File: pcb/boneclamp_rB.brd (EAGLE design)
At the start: 160 x 100 mm, 65 parts, among them IC1 24C, U1 AD7656YSTZ, U2 AD5754RBREZ, U3 SN74ABT541BDW, U4 ADP3303ARZ-5, U5 ADP3303ARZ-5, U6 ADR431BRZ, U7 AD7682BCPZ

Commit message: More changes to circuit
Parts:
- removed U$26: LM1085, boneclamp:TO263-3
- removed U$28: SCREW3, boneclamp:SCREW3
- added C21: 0.1uF, rcl:C0603
- added C25, C28: 10uF, rcl:C1206
- added U8: TPS63700DRCT, ti-extended:SON50P300X300X100-11N
- C19, C20: value 10uF -> 0.1uF; device rcl:C1206 -> rcl:C0603
- U2: value AD5754RBREZ -> ADP3303ARZ-5; device analog-devices-01:SOP65P640X120-25N -> analog-devices-01:SOIC127P600X175-8N
- moved C20 148.6 mm to (-85.1, -52.1)
- moved C19 137.1 mm to (-72.4, -44.5)
- moved U2 134.0 mm to (-82.5, -35.6), turned to 0 degrees
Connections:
- removed net +12V: C19.1, U$26.3
- removed net -12V: U$28.P$3
- removed net EPAD: U2.25
- removed net PGND: U$28.P$2
- new net AVSS: C20.1, C21.1, C28.1, U2.1, U2.2
- new net N$26: C20.2, U2.3
- new net VIN: U8.3
- net AGND: now also C19.2, C21.2, C25.2, C28.2, U2.4
- net BB_5V: now also C19.1, C25.1, U2.5, U2.7, U2.8
- net DAC_A: no longer U2.3
- net DAC_B: no longer U2.4
- net DAC_C: no longer U2.23
- net DAC_D: no longer U2.22
- net DGND: no longer C19.2, C20.2, U$26.1
- net DVCC: no longer U2.14
- net N$24: no longer U2.17
- net N$7: no longer U2.16
- net N$8: no longer U2.9
- net VDD: no longer U2.24
- net VDD_BB: no longer C20.1, U$26.2, U$26.TAB
- net VSS: no longer U2.1

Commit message: Worked a bit on the schematic
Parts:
- removed C23: 10uF, rcl:C1206
- removed C24, C26, C27: 0.1uF, rcl:C0603
- removed JP5: (no value), jumper:JP2
- removed JP6: (no value), jumper:JP1
- removed TP5: TPB1,27, testpad:B1,27
- removed U3: SN74ABT541BDW, ti-extended:SOIC127P1030X265-20N
- removed U6: ADR431BRZ, analog-devices-01:SOIC127P600X175-8N
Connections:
- removed net N$23: JP6.1
- removed net N$25: C26.1, U6.1
- removed net VCC: U3.20
- removed net VREF_OUT: C27.1, JP5.3, JP6.2, TP5.TP, U6.6
- net AGND: no longer C23.2, C24.2, C26.2, U6.4
- net VDD: no longer C23.1, C24.1, U6.2
- net VREF_2.5V: no longer JP5.2
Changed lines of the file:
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@@
 <attribute name="OC_FARNELL" value="1274233" x="194.31" y="153.67" size="1.778" layer="27" rot="R90" display="off"/>
-</element>
-<element name="U3" library="ti-extended" package="SOIC127P1030X265-20N" value="SN74ABT541BDW" x="76.2" y="19.05" rot="R90">
-<attribute name="PACKAGE" value="SOIC-20" x="173.99" y="109.22" size="1.778" layer="27" rot="R90" display="off"/>
-<attribute name="OC_NEWARK" value="85F222" x="173.99" y="109.22" size="1.778" layer="27" rot="R90" display="off"/>
-<attribute name="MPN" value="SN74ABT541BDW" x="173.99" y="109.22" size="1.778" layer="27" rot="R90" display="off"/>
-<attribute name="SUPPLIER" value="Texas Instruments" x="173.99" y="109.22" size="1.778" layer="27" rot="R90" display="off"/>
-<attribute name="OC_FARNELL" value="9590170" x="173.99" y="109.22" size="1.778" layer="27" rot="R90" display="off"/>
 </element>
 <element name="BCIO" library="adafruit" package="HDF15H" value="F15-SHEILD" x="27.305" y="74.93" rot="R180"/>
@@
 <element name="JP3" library="jumper" package="JP1" value="" x="6.35" y="-16.51"/>
 <element name="JP4" library="jumper" package="JP1" value="" x="6.35" y="-24.13"/>
-<element name="U6" library="analog-devices-01" package="SOIC127P600X175-8N" value="ADR431BRZ" x="-46.99" y="48.26">
-<attribute name="PACKAGE" value="SOIC-8" x="-46.99" y="48.26" size="1.778" layer="27" display="off"/>
-<attribute name="OC_NEWARK" value="12M8194" x="-46.99" y="48.26" size="1.778" layer="27" display="off"/>
-<attribute name="MPN" value="ADR431BRZ" x="-46.99" y="48.26" size="1.778" layer="27" display="off"/>
-<attribute name="SUPPLIER" value="Analog Devices" x="-46.99" y="48.26" size="1.778" layer="27" display="off"/>
-<attribute name="OC_FARNELL" value="1498664" x="-46.99" y="48.26" size="1.778" layer="27" display="off"/>
-</element>
-<element name="C24" library="rcl" package="C0603" value="0.1uF" x="-53.34" y="45.72" rot="R270"/>
-<element name="C26" library="rcl" package="C0603" value="0.1uF" x="-53.34" y="50.8" rot="R270"/>
-<element name="C27" library="rcl" package="C0603" value="0.1uF" x="-40.64" y="49.53" rot="R90"/>
 <element name="C5" library="rcl" package="C1206" value="10uF" x="-55.88" y="50.8" rot="R270"/>
 <element name="C8" library="rcl" package="C1206" value="10uF" x="-11.43" y="26.67"/>
 <element name="C10" library="rcl" package="C1206" value="10uF" x="-11.43" y="20.32"/>
 <element name="C13" library="rcl" package="C1206" value="10uF" x="-11.43" y="13.97"/>
-<element name="C23" library="rcl" package="C1206" value="10uF" x="-11.43" y="1.27"/>
-<element name="TP5" library="testpad" package="B1,27" value="TPB1,27" x="-12.7" y="-5.08">
-<attribute name="TP_SIGNAL_NAME" value="" x="-12.7" y="-5.08" size="1.778" layer="27" display="off"/>
-</element>
-<element name="JP5" library="jumper" package="JP2" value="" x="-19.05" y="-1.27"/>
-<element name="JP6" library="jumper" package="JP1" value="" x="-26.67" y="-2.54"/>
 <element name="U$42" library="analog-devices-02" package="MO-153-AB" value="AD5686RARUZ" x="-68.58" y="-20.32"/>
 <element name="U7" library="analog-devices-02" package="QFN50P400X400X100-21N" value="AD7682BCPZ" x="-82.55" y="-20.32">
@@
 <signal name="VDD">
 <contactref element="U1" pad="31"/>
-<contactref element="U6" pad="2"/>
-<contactref element="C24" pad="1"/>
-<contactref element="C23" pad="1"/>
 <contactref element="U$42" pad="5"/>
 <contactref element="U7" pad="20"/>
-<wire x1="-12.83" y1="1.27" x2="99.695" y2="95.9612" width="0" layer="19" extent="1-1"/>
-<wire x1="-49.4538" y1="48.895" x2="-12.83" y2="1.27" width="0" layer="19" extent="1-1"/>
-<wire x1="-53.34" y1="46.57" x2="-49.4538" y2="48.895" width="0" layer="19" extent="1-1"/>
-<wire x1="-71.3994" y1="-20.6502" x2="-12.83" y2="1.27" width="0" layer="19" extent="1-1"/>
+<wire x1="-71.3994" y1="-20.6502" x2="99.695" y2="95.9612" width="0" layer="19" extent="1-1"/>
 <wire x1="-83.5406" y1="-18.542" x2="-71.3994" y2="-20.6502" width="0" layer="19" extent="1-1"/>
 </signal>
@@
 <wire x1="38.52" y1="25.4" x2="32.17" y2="25.4" width="0" layer="19" extent="1-1"/>
 <wire x1="-12.83" y1="13.97" x2="32.17" y2="25.4" width="0" layer="19" extent="1-1"/>
-</signal>
-<signal name="VCC">
-<contactref element="U3" pad="20"/>
 </signal>
 <signal name="N$1">
@@
 <contactref element="C16" pad="2"/>
 <contactref element="SJ4" pad="1"/>
-<contactref element="U6" pad="4"/>
-<contactref element="C24" pad="2"/>
-<contactref element="C26" pad="2"/>
 <contactref element="C5" pad="2"/>
 <contactref element="C10" pad="2"/>
-<contactref element="C23" pad="2"/>
 <contactref element="U2" pad="4"/>
 <contactref element="C19" pad="2"/>
@@
 <wire x1="1.905" y1="19.05" x2="4.445" y2="19.05" width="0" layer="19" extent="1-1"/>
 <wire x1="-10.03" y1="20.32" x2="1.905" y2="19.05" width="0" layer="19" extent="1-1"/>
-<wire x1="-10.03" y1="1.27" x2="-10.03" y2="20.32" width="0" layer="19" extent="1-1"/>
-<wire x1="-49.4538" y1="46.355" x2="-10.03" y2="20.32" width="0" layer="19" extent="1-1"/>
-<wire x1="-53.34" y1="44.87" x2="-49.4538" y2="46.355" width="0" layer="19" extent="1-1"/>
-<wire x1="-53.34" y1="49.95" x2="-53.34" y2="44.87" width="0" layer="19" extent="1-1"/>
-<wire x1="-55.88" y1="49.4" x2="-53.34" y2="49.95" width="0" layer="19" extent="1-1"/>
-<wire x1="-71.54" y1="-44.45" x2="-10.03" y2="1.27" width="0" layer="19" extent="1-1"/>
+<wire x1="-55.88" y1="49.4" x2="-10.03" y2="20.32" width="0" layer="19" extent="1-1"/>
+<wire x1="-71.54" y1="-44.45" x2="-10.03" y2="20.32" width="0" layer="19" extent="1-1"/>
 <wire x1="-76.07" y1="-45.72" x2="-71.54" y2="-44.45" width="0" layer="19" extent="1-1"/>
 <wire x1="-82.42" y1="-45.72" x2="-76.07" y2="-45.72" width="0" layer="19" extent="1-1"/>
@@
 <contactref element="JP3" pad="2"/>
 <contactref element="JP4" pad="2"/>
-<contactref element="JP5" pad="2"/>
-<wire x1="6.35" y1="-22.86" x2="-19.05" y2="-1.27" width="0" layer="19" extent="1-1"/>
 <wire x1="6.35" y1="-15.24" x2="6.35" y2="-22.86" width="0" layer="19" extent="1-1"/>
 </signal>
@@
 <contactref element="JP4" pad="1"/>
 </signal>
-<signal name="N$25">
-<contactref element="U6" pad="1"/>
-<contactref element="C26" pad="1"/>
-<wire x1="-49.4538" y1="50.165" x2="-53.34" y2="51.65" width="0" layer="19" extent="1-1"/>
-</signal>
-<signal name="VREF_OUT">
-<contactref element="U6" pad="6"/>
-<contactref element="C27" pad="1"/>
-<contactref element="TP5" pad="TP"/>
-<contactref element="JP5" pad="3"/>
-<contactref element="JP6" pad="2"/>
-<wire x1="-16.51" y1="-1.27" x2="-12.7" y2="-5.08" width="0" layer="19" extent="1-1"/>
-<wire x1="-26.67" y1="-1.27" x2="-16.51" y2="-1.27" width="0" layer="19" extent="1-1"/>
-<wire x1="-40.64" y1="48.68" x2="-16.51" y2="-1.27" width="0" layer="19" extent="1-1"/>
-<wire x1="-44.5262" y1="47.625" x2="-40.64" y2="48.68" width="0" layer="19" extent="1-1"/>
-</signal>
-<signal name="N$23">
-<contactref element="JP6" pad="1"/>
-</signal>
 <signal name="VDD_2">

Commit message: Wired the DC-DC inverter
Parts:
- added C23: 10uF, rcl:C0805
- added C24: 22nF, rcl:C0805
- added C26: 0.1uF, rcl:C0805
- added C27: 4.7nF, rcl:C0805
- added C29: 10nF, rcl:C0805
- added C30, C31, C32, C33: 4.7uF, rcl:C0805
- added C34: 0.22uF, rcl:C0805
- added C35: 10pF, rcl:C0805
- added R12: 750, resistor:R0805
- added R13: 150k, resistor:R0805
- added R5: 100k, resistor:R0805
- added U$27: (no value), boneclamp:DO-219AB
- added U$28: 4.7uH, boneclamp:L4012M
- C15, C16, C17, C18: device rcl:C0603 -> rcl:C0805
- R1, R2, R3, R4: device rcl:R0603 -> rcl:R0805
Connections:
- removed net VDD_BB: U$1.51, U$1.52
- removed net VIN: U8.3
- new net N$23: C26.1, R5.2, U8.3, U8.4
- new net N$25: C27.1, U8.1
- new net N$27: U$27.P$1, U$28.1, U8.6
- new net N$30: C35.1, R12.2, R13.1, U8.9
- new net N$31: C34.1, R13.2, U8.10
- new net SYS_5V: U$1.53
- new net VDD_5V: C23.1, C24.1, R5.1, U$1.51, U$1.52, U8.5
- new net _VSS: C29.1, C30.1, C31.1, C32.1, C33.1, C35.2, R12.1, U$27.P$2, U8.8
- net AGND: now also C23.2, C24.2, C26.2, C27.2, C29.2, C30.2, C31.2, C32.2, C33.2, C34.2, U$28.2, U8.11, U8.2, U8.7
- net BB_5V: no longer U$1.53, U$1.54
- net DAC_A: now also C15.1, R1.2, TP4.TP; no longer C18.1, R4.2, TP1.TP
- net DAC_B: now also C16.1, R2.2, TP3.TP; no longer C17.1, R3.2, TP2.TP
- net DAC_C: now also C17.1, R3.2, TP2.TP; no longer C16.1, R2.2, TP3.TP
- net DAC_D: now also C18.1, R4.2, TP1.TP; no longer C15.1, R1.2, TP4.TP

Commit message: Added negative LDO regulator
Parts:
- removed C10, C13, C25, C28, C8: 10uF, rcl:C1206
- removed C11, C12, C14, C19, C20, C21, C9: 0.1uF, rcl:C0603
- removed U4, U5: ADP3303ARZ-5, analog-devices-01:SOIC127P600X175-8N
- C5: value 10uF -> 1uF; device rcl:C1206 -> rcl:C0805
- C6: value 0.1uF -> 0.01uF; device rcl:C0603 -> rcl:C0805
- C7: value 0.1uF -> 10uF; device rcl:C0603 -> rcl:C0805
- U2: value ADP3303ARZ-5 -> LT1964ES5-5TRMPBF; device analog-devices-01:SOIC127P600X175-8N -> linear-extended-01:SOT95P280X100-5N
- moved C7 268.9 mm to (-83.8, -190.5)
- moved C6 267.7 mm to (-83.8, -184.2)
- moved C5 230.3 mm to (-83.8, -177.8), turned to 0 degrees
- moved U2 133.3 mm to (-82.5, -168.9)
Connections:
- removed net AVCC: C10.1, C7.1, C9.1, U4.1, U4.2
- removed net AVSS: C20.1, C21.1, C28.1, U2.1, U2.2
- removed net BB_5V: C11.1, C19.1, C25.1, C5.1, C6.1, C8.1, U2.5, U2.7, U2.8, U4.5, U4.7, U4.8, U5.5, U5.7, U5.8
- removed net N$15: C12.2, U5.3
- removed net N$26: C20.2, U2.3
- net AGND: now also C7.2, U2.1; no longer C10.2, C19.2, C21.2, C25.2, C28.2, C9.2, U2.4, U4.4, U5.4
- net DAC_A: now also U$42.3
- net DAC_B: now also U$42.2
- net DAC_C: now also U$42.6
- net DAC_D: now also U$42.7
- net DGND: no longer C11.2, C13.2, C14.2, C8.2
- net DVCC: no longer C12.1, C13.1, C14.1, U5.1, U5.2
- net N$16: now also C6.1, U2.3; no longer C7.2, U4.3
- net N$24: now also U$42.1
- net N$7: now also U$42.8
- net N$8: now also U$42.14
- net VDRIVE: now also U$42.11
- net VSS: now also C7.1, U2.5
- net _VSS: now also C5.1, U2.2, U2.4

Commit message: Minor schematic edit
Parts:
- added U3: LT1962EMS8-5PBF, linear-extended-01:SOP65P490X110-8N
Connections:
- new net IN: U3.8
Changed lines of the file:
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@@
 <element name="C6" library="rcl" package="C0805" value="0.01uF" x="-83.82" y="-184.15"/>
 <element name="C7" library="rcl" package="C0805" value="10uF" x="-83.82" y="-190.5"/>
+<element name="U3" library="linear-extended-01" package="SOP65P490X110-8N" value="LT1962EMS8-5PBF" x="-82.55" y="-199.39">
+<attribute name="PACKAGE" value="MSOP-8" x="-82.55" y="-199.39" size="1.778" layer="27" display="off"/>
+<attribute name="OC_NEWARK" value="57M7401" x="-82.55" y="-199.39" size="1.778" layer="27" display="off"/>
+<attribute name="MPN" value="LT1962EMS8-5#PBF" x="-82.55" y="-199.39" size="1.778" layer="27" display="off"/>
+<attribute name="SUPPLIER" value="Linear Technologies" x="-82.55" y="-199.39" size="1.778" layer="27" display="off"/>
+<attribute name="OC_FARNELL" value="1273624" x="-82.55" y="-199.39" size="1.778" layer="27" display="off"/>
+</element>
 </elements>
 <signals>
@@
 <wire x1="-84.77" y1="-184.15" x2="-83.7692" y2="-169.8498" width="0" layer="19" extent="1-1"/>
 </signal>
+<signal name="IN">
+<contactref element="U3" pad="8"/>
+</signal>
 </signals>

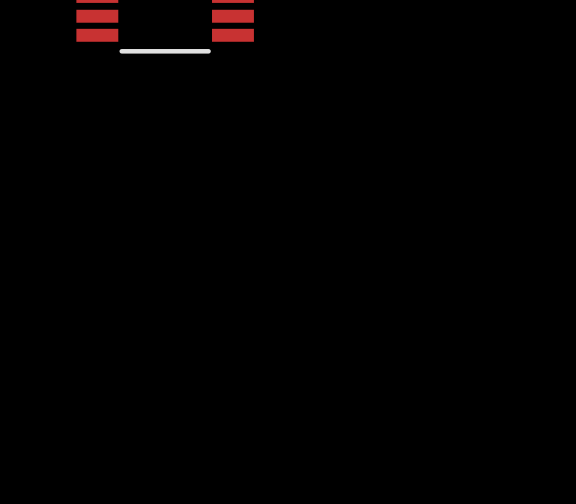
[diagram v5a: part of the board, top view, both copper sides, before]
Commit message: Added data sheets for the smd-to-dip adapters we will use. Minor changes to schematic
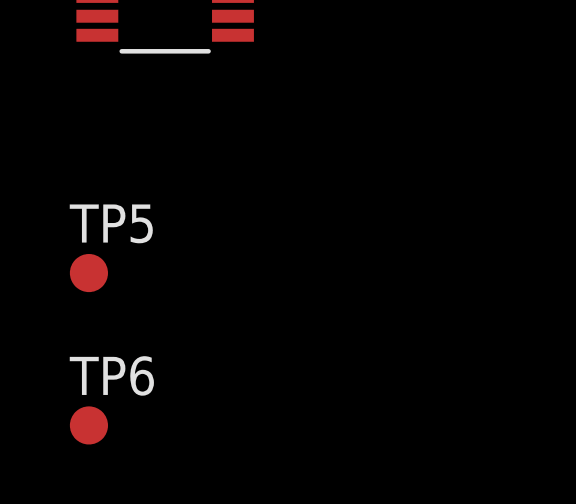
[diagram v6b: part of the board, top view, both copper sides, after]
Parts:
- added TP5, TP6: TPB1,27, testpad:B1,27
- C6: value 0.01uF -> 10nF
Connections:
- net VDRIVE: now also TP6.TP
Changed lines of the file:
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@@
 </element>
 <element name="C5" library="rcl" package="C0805" value="1uF" x="-83.82" y="-177.8"/>
-<element name="C6" library="rcl" package="C0805" value="0.01uF" x="-83.82" y="-184.15"/>
+<element name="C6" library="rcl" package="C0805" value="10nF" x="-83.82" y="-184.15"/>
 <element name="C7" library="rcl" package="C0805" value="10uF" x="-83.82" y="-190.5"/>
 <element name="U3" library="linear-extended-01" package="SOP65P490X110-8N" value="LT1962EMS8-5PBF" x="-82.55" y="-199.39">
@@
 <attribute name="SUPPLIER" value="Linear Technologies" x="-82.55" y="-199.39" size="1.778" layer="27" display="off"/>
 <attribute name="OC_FARNELL" value="1273624" x="-82.55" y="-199.39" size="1.778" layer="27" display="off"/>
+</element>
+<element name="TP5" library="testpad" package="B1,27" value="TPB1,27" x="-85.09" y="-208.28">
+<attribute name="TP_SIGNAL_NAME" value="" x="-85.09" y="-208.28" size="1.778" layer="27" display="off"/>
+</element>
+<element name="TP6" library="testpad" package="B1,27" value="TPB1,27" x="-85.09" y="-213.36">
+<attribute name="TP_SIGNAL_NAME" value="" x="-85.09" y="-213.36" size="1.778" layer="27" display="off"/>
 </element>
 </elements>
@@
 <contactref element="R10" pad="2"/>
 <contactref element="U$42" pad="11"/>
+<contactref element="TP6" pad="TP"/>
 <wire x1="13.55" y1="-5.08" x2="-65.7606" y2="-21.2852" width="0" layer="19" extent="1-1"/>
 <wire x1="13.55" y1="0" x2="13.55" y2="-5.08" width="0" layer="19" extent="1-1"/>
@@
 <wire x1="50.165" y1="21.59" x2="34.29" y2="30.48" width="0" layer="19" extent="1-1"/>
 <wire x1="52.705" y1="21.59" x2="50.165" y2="21.59" width="0" layer="19" extent="1-1"/>
+<wire x1="-85.09" y1="-213.36" x2="-65.7606" y2="-21.2852" width="0" layer="19" extent="1-1"/>
 </signal>
 <signal name="N$13">
